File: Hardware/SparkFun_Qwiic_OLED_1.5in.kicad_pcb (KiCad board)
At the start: 2 copper layers, 34.3 x 49.5 mm, 69 parts, among them J1 Qwiic_RA, J2 Qwiic_RA, J4 Conn_01x24_FPC, J5 Conn_01x07, U2 WEO128128ASAP3N00000, U5 AP3012

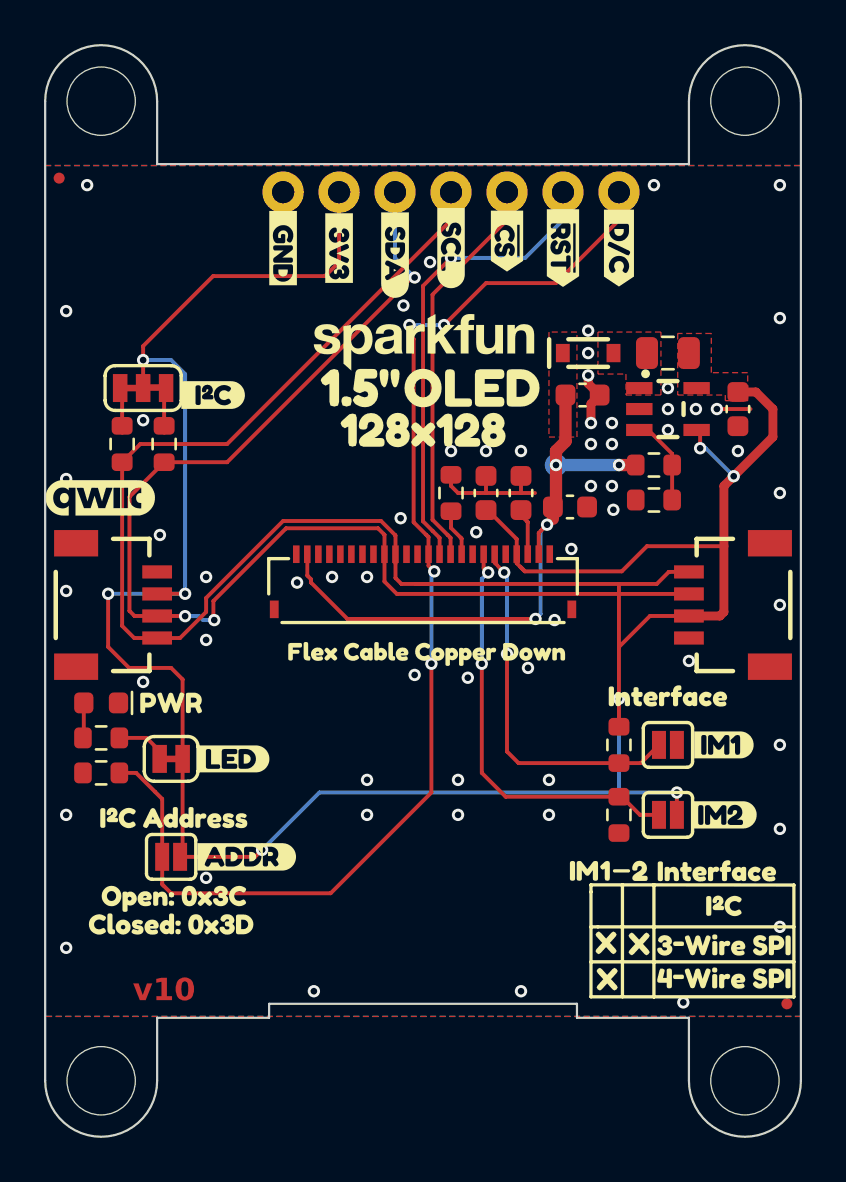
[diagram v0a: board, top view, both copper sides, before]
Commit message: Centers PTH headers and screen, fixes some DRC errors created by moving the FPC connector over that small amount
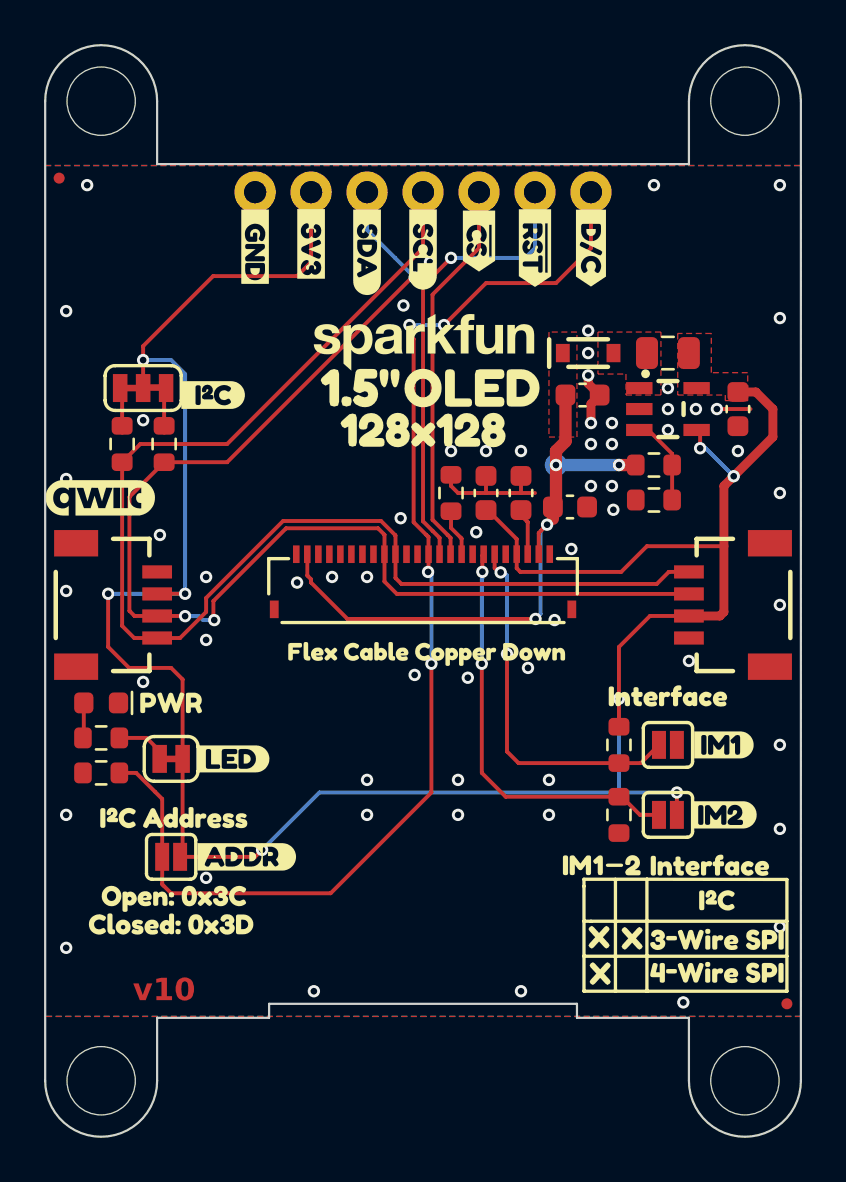
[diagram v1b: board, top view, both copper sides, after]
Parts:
- moved kibuzzard-67BF7ED9 1.28 mm to (135.3, 70.3)
- moved kibuzzard-67BF7F13 1.28 mm to (137.9, 70.7)
- moved kibuzzard-67BF7EBF 1.27 mm to (132.8, 70.4)
- moved kibuzzard-67BF7F2F 1.27 mm to (140.4, 70.5)
- moved J5 1.27 mm to (132.8, 67.9)
- moved kibuzzard-680E7A69 1.27 mm to (143.0, 70.2)
- moved kibuzzard-680E7A4B 1.27 mm to (145.5, 70.5)
- moved kibuzzard-685B1775 1.27 mm to (148.0, 70.5)
- moved kibuzzard-6893822D 0.41 mm to (147.4, 98.5)
- moved kibuzzard-689381EF 0.41 mm to (148.4, 103.4)
- moved kibuzzard-689381EF 0.41 mm to (148.4, 101.8)
- moved kibuzzard-68938236 0.41 mm to (148.3, 98.5)
- moved kibuzzard-68938244 0.41 mm to (153.4, 98.5)
- moved kibuzzard-6893824B 0.41 mm to (149.9, 98.5)
- moved kibuzzard-68938257 0.41 mm to (153.7, 100.1)
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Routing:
- net 3.3V: track 116.7 -> 112.5 mm
- net SCL/SCK: track 59.7 -> 58.7 mm
- net ~{CS}: track 18.2 -> 17.6 mm
- net ~{RST}: track 21.3 -> 20.8 mm
- net SDA/SDI: track 56.9 -> 57.4 mm

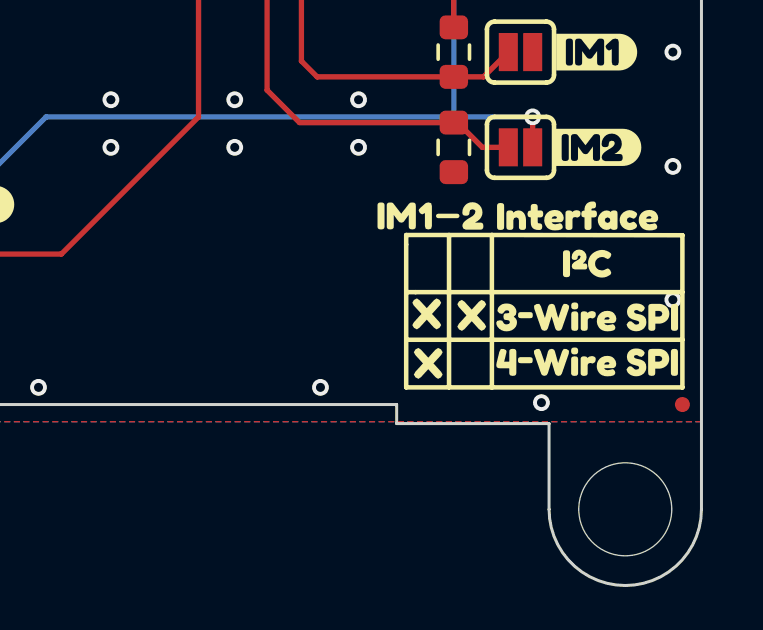
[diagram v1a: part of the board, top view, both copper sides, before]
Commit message: Adds some "O"'s to indicate open on the interface table
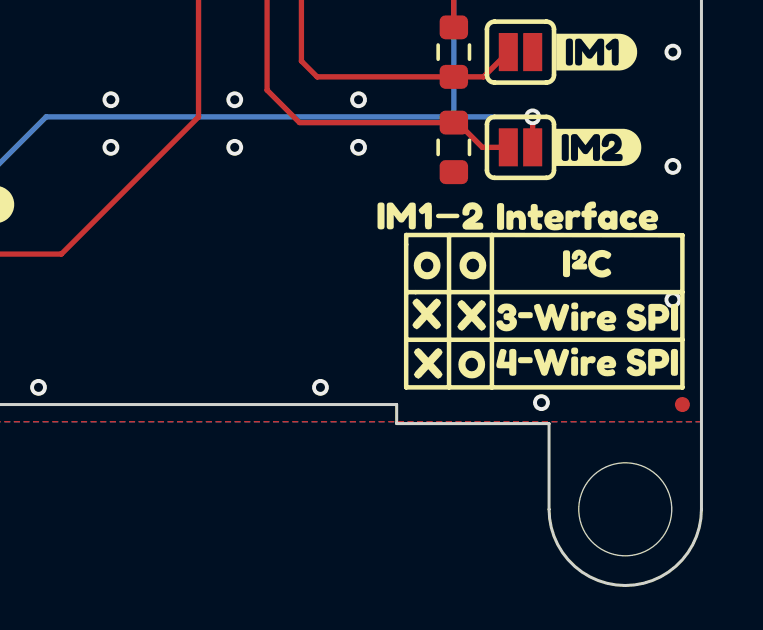
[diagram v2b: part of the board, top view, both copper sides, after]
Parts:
- added kibuzzard-6893A61C: G***, kibuzzard-6893A61C, F.Cu at (148.4, 100.1)
- added kibuzzard-6893A61C: G***, kibuzzard-6893A61C, F.Cu at (149.9, 103.4)
- added kibuzzard-6893A61C: G***, kibuzzard-6893A61C, F.Cu at (149.9, 100.1)
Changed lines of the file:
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@@
 		(embedded_fonts no)
 	)
+	(footprint "kibuzzard-6893A61C"
+		(layer "F.Cu")
+		(at 148.412 100.138)
+		(descr "Generated with KiBuzzard")
+		(tags "kb_params=eyJBbGlnbm1lbnRDaG9pY2UiOiAiQ2VudGVyIiwgIkNhcExlZnRDaG9pY2UiOiAiKCIsICJDYXBSaWdodENob2ljZSI6ICJdIiwgIkZvbnRDb21ib0JveCI6ICJGcmVkZHlTcGFyay1SZWd1bGFyIiwgIkhlaWdodEN0cmwiOiAwLjksICJMYXllckNvbWJvQm94IjogIkYuU2lsa1MiLCAiTGluZVNwYWNpbmdDdHJsIjogMS41LCAiTXVsdGlMaW5lVGV4dCI6ICJPIiwgIlBhZGRpbmdCb3R0b21DdHJsIjogMS41LCAiUGFkZGluZ0xlZnRDdHJsIjogMy4wLCAiUGFkZGluZ1JpZ2h0Q3RybCI6IDAuMCwgIlBhZGRpbmdUb3BDdHJsIjogMS41LCAiV2lkdGhDdHJsIjogMS4wLCAiYWR2YW5jZWRDaGVja2JveCI6IHRydWUsICJpbmxpbmVGb3JtYXRUZXh0Ym94IjogdHJ1ZSwgImxpbmVvdmVyU3R5bGVDaG9pY2UiOiAiU3F1YXJlIiwgImxpbmVvdmVyVGhpY2tuZXNzQ3RybCI6IDF9")
+		(property "Reference" "kibuzzard-6893A61C"
+			(at 0 -3.510876 0)
+			(layer "F.SilkS")
+			(hide yes)
+			(effects
+				(font
+					(size 0.001 0.001)
+				)
+			)
+		)
+		(property "Value" "G***"
+			(at 0 3.510876 0)
+			(layer "F.SilkS")
+			(hide yes)
+			(effects
+				(font
+					(size 0.001 0.001)
+				)
+			)
+		)
+		(property "Datasheet" ""
+			(at 0 0 0)
+			(layer "F.Fab")
+			(hide yes)
+			(effects
+				(font
+					(size 1.27 1.27)
+					(thickness 0.15)
+				)
+			)
+		)
+		(property "Description" ""
+			(at 0 0 0)
+			(layer "F.Fab")
+			(hide yes)
+			(effects
+				(font
+					(size 1.27 1.27)
+					(thickness 0.15)
+				)
+			)
+		)
+		(attr board_only exclude_from_pos_files exclude_from_bom)
+		(fp_poly
+			(pts
+				(xy 0.005794 0.462876) (xy -0.000644 0.462277) (xy -0.000644 0.227253) (xy 0.081277 0.210998) (xy 0.149356 0.162232)
+				(xy 0.195225 0.089324) (xy 0.210515 0.000644) (xy 0.195064 -0.087393) (xy 0.148712 -0.160944) (xy 0.080794 -0.210676)
+				(xy 0.000644 -0.227253) (xy -0.080472 -0.210676) (xy -0.148712 -0.160944) (xy -0.195064 -0.087393)
+				(xy -0.210515 0.000644) (xy -0.194903 0.08691) (xy -0.148069 0.1603) (xy -0.079989 0.210515) (xy -0.000644 0.227253)
+				(xy -0.000644 0.462277) (xy -0.084174 0.454506) (xy -0.167382 0.429399) (xy -0.24383 0.387554) (xy -0.313519 0.32897)
+				(xy -0.37154 0.258557) (xy -0.412983 0.181223) (xy -0.437849 0.096969) (xy -0.446137 0.005794) (xy -0.43809 -0.088358)
+				(xy -0.413948 -0.175107) (xy -0.373712 -0.254453) (xy -0.317382 -0.326395) (xy -0.249544 -0.386105)
+				(xy -0.174785 -0.428755) (xy -0.093106 -0.454345) (xy -0.004506 -0.462876) (xy 0.085944 -0.454466)
+				(xy 0.169313 -0.429238) (xy 0.245601 -0.387192) (xy 0.314807 -0.328326) (xy 0.372264 -0.25731) (xy 0.413305 -0.178809)
+				(xy 0.437929 -0.092825) (xy 0.446137 0.000644) (xy 0.43805 0.092503) (xy 0.413788 0.177521) (xy 0.37335 0.2557)
+				(xy 0.316738 0.327039) (xy 0.24878 0.386467) (xy 0.174303 0.428916) (xy 0.093307 0.454386) (xy 0.005794 0.462876)
+			)
+			(stroke
+				(width 0)
+				(type solid)
+			)
+			(fill yes)
+			(layer "F.SilkS")
+		)
+		(embedded_fonts no)
+	)
 	(footprint "SparkFun-Resistor:R_0603_1608Metric"
 		(layer "F.Cu")
@@
 		)
 	)
+	(footprint "kibuzzard-6893A61C"
+		(layer "F.Cu")
+		(at 149.8985 103.44)
+		(descr "Generated with KiBuzzard")
+		(tags "kb_params=eyJBbGlnbm1lbnRDaG9pY2UiOiAiQ2VudGVyIiwgIkNhcExlZnRDaG9pY2UiOiAiKCIsICJDYXBSaWdodENob2ljZSI6ICJdIiwgIkZvbnRDb21ib0JveCI6ICJGcmVkZHlTcGFyay1SZWd1bGFyIiwgIkhlaWdodEN0cmwiOiAwLjksICJMYXllckNvbWJvQm94IjogIkYuU2lsa1MiLCAiTGluZVNwYWNpbmdDdHJsIjogMS41LCAiTXVsdGlMaW5lVGV4dCI6ICJPIiwgIlBhZGRpbmdCb3R0b21DdHJsIjogMS41LCAiUGFkZGluZ0xlZnRDdHJsIjogMy4wLCAiUGFkZGluZ1JpZ2h0Q3RybCI6IDAuMCwgIlBhZGRpbmdUb3BDdHJsIjogMS41LCAiV2lkdGhDdHJsIjogMS4wLCAiYWR2YW5jZWRDaGVja2JveCI6IHRydWUsICJpbmxpbmVGb3JtYXRUZXh0Ym94IjogdHJ1ZSwgImxpbmVvdmVyU3R5bGVDaG9pY2UiOiAiU3F1YXJlIiwgImxpbmVvdmVyVGhpY2tuZXNzQ3RybCI6IDF9")
+		(property "Reference" "kibuzzard-6893A61C"
+			(at 0 -3.510876 0)
+			(layer "F.SilkS")
+			(hide yes)
+			(effects
+				(font
+					(size 0.001 0.001)
+					(thickness 0.15)
+				)
+			)
+		)
+		(property "Value" "G***"
+			(at 0 3.510876 0)
+			(layer "F.SilkS")
+			(hide yes)
+			(effects
+				(font
+					(size 0.001 0.001)
+					(thickness 0.15)
+				)
+			)
+		)
+		(property "Datasheet" ""
+			(at 0 0 0)
+			(layer "F.Fab")
+			(hide yes)
+			(effects
+				(font
+					(size 1.27 1.27)
+					(thickness 0.15)
+				)
+			)
+		)
+		(property "Description" ""
+			(at 0 0 0)
+			(layer "F.Fab")
+			(hide yes)
+			(effects
+				(font
+					(size 1.27 1.27)
+					(thickness 0.15)
+				)
+			)
+		)
+		(attr board_only exclude_from_pos_files exclude_from_bom)
+		(fp_poly
+			(pts
+				(xy 0.005794 0.462876) (xy -0.000644 0.462277) (xy -0.000644 0.227253) (xy 0.081277 0.210998) (xy 0.149356 0.162232)
+				(xy 0.195225 0.089324) (xy 0.210515 0.000644) (xy 0.195064 -0.087393) (xy 0.148712 -0.160944) (xy 0.080794 -0.210676)
+				(xy 0.000644 -0.227253) (xy -0.080472 -0.210676) (xy -0.148712 -0.160944) (xy -0.195064 -0.087393)
+				(xy -0.210515 0.000644) (xy -0.194903 0.08691) (xy -0.148069 0.1603) (xy -0.079989 0.210515) (xy -0.000644 0.227253)
+				(xy -0.000644 0.462277) (xy -0.084174 0.454506) (xy -0.167382 0.429399) (xy -0.24383 0.387554) (xy -0.313519 0.32897)
+				(xy -0.37154 0.258557) (xy -0.412983 0.181223) (xy -0.437849 0.096969) (xy -0.446137 0.005794) (xy -0.43809 -0.088358)
+				(xy -0.413948 -0.175107) (xy -0.373712 -0.254453) (xy -0.317382 -0.326395) (xy -0.249544 -0.386105)
+				(xy -0.174785 -0.428755) (xy -0.093106 -0.454345) (xy -0.004506 -0.462876) (xy 0.085944 -0.454466)
+				(xy 0.169313 -0.429238) (xy 0.245601 -0.387192) (xy 0.314807 -0.328326) (xy 0.372264 -0.25731) (xy 0.413305 -0.178809)
+				(xy 0.437929 -0.092825) (xy 0.446137 0.000644) (xy 0.43805 0.092503) (xy 0.413788 0.177521) (xy 0.37335 0.2557)
+				(xy 0.316738 0.327039) (xy 0.24878 0.386467) (xy 0.174303 0.428916) (xy 0.093307 0.454386) (xy 0.005794 0.462876)
+			)
+			(stroke
+				(width 0)
+				(type solid)
+			)
+			(fill yes)
+			(layer "F.SilkS")
+		)
+		(embedded_fonts no)
+	)
 	(footprint "SparkFun-Jumper:Jumper_3_NC-2_Trace"
 		(layer "F.Cu")
@@
 			)
 			(stroke
+				(width 0)
+				(type solid)
+			)
+			(fill yes)
+			(layer "F.SilkS")
+		)
+		(embedded_fonts no)
+	)
+	(footprint "kibuzzard-6893A61C"
+		(layer "F.Cu")
+		(at 149.936 100.138)
+		(descr "Generated with KiBuzzard")
+		(tags "kb_params=eyJBbGlnbm1lbnRDaG9pY2UiOiAiQ2VudGVyIiwgIkNhcExlZnRDaG9pY2UiOiAiKCIsICJDYXBSaWdodENob2ljZSI6ICJdIiwgIkZvbnRDb21ib0JveCI6ICJGcmVkZHlTcGFyay1SZWd1bGFyIiwgIkhlaWdodEN0cmwiOiAwLjksICJMYXllckNvbWJvQm94IjogIkYuU2lsa1MiLCAiTGluZVNwYWNpbmdDdHJsIjogMS41LCAiTXVsdGlMaW5lVGV4dCI6ICJPIiwgIlBhZGRpbmdCb3R0b21DdHJsIjogMS41LCAiUGFkZGluZ0xlZnRDdHJsIjogMy4wLCAiUGFkZGluZ1JpZ2h0Q3RybCI6IDAuMCwgIlBhZGRpbmdUb3BDdHJsIjogMS41LCAiV2lkdGhDdHJsIjogMS4wLCAiYWR2YW5jZWRDaGVja2JveCI6IHRydWUsICJpbmxpbmVGb3JtYXRUZXh0Ym94IjogdHJ1ZSwgImxpbmVvdmVyU3R5bGVDaG9pY2UiOiAiU3F1YXJlIiwgImxpbmVvdmVyVGhpY2tuZXNzQ3RybCI6IDF9")
+		(property "Reference" "kibuzzard-6893A61C"
+			(at 0 -3.510876 0)
+			(layer "F.SilkS")
+			(hide yes)
+			(effects
+				(font
+					(size 0.001 0.001)
+					(thickness 0.15)
+				)
+			)
+		)
+		(property "Value" "G***"
+			(at 0 3.510876 0)
+			(layer "F.SilkS")
+			(hide yes)
+			(effects
+				(font
+					(size 0.001 0.001)
+					(thickness 0.15)
+				)
+			)
+		)
+		(property "Datasheet" ""
+			(at 0 0 0)
+			(layer "F.Fab")
+			(hide yes)
+			(effects
+				(font
+					(size 1.27 1.27)
+					(thickness 0.15)
+				)
+			)
+		)
+		(property "Description" ""
+			(at 0 0 0)
+			(layer "F.Fab")
+			(hide yes)
+			(effects
+				(font
+					(size 1.27 1.27)
+					(thickness 0.15)
+				)
+			)
+		)
+		(attr board_only exclude_from_pos_files exclude_from_bom)
+		(fp_poly
+			(pts
+				(xy 0.005794 0.462876) (xy -0.000644 0.462277) (xy -0.000644 0.227253) (xy 0.081277 0.210998) (xy 0.149356 0.162232)
+				(xy 0.195225 0.089324) (xy 0.210515 0.000644) (xy 0.195064 -0.087393) (xy 0.148712 -0.160944) (xy 0.080794 -0.210676)
+				(xy 0.000644 -0.227253) (xy -0.080472 -0.210676) (xy -0.148712 -0.160944) (xy -0.195064 -0.087393)
+				(xy -0.210515 0.000644) (xy -0.194903 0.08691) (xy -0.148069 0.1603) (xy -0.079989 0.210515) (xy -0.000644 0.227253)
+				(xy -0.000644 0.462277) (xy -0.084174 0.454506) (xy -0.167382 0.429399) (xy -0.24383 0.387554) (xy -0.313519 0.32897)
+				(xy -0.37154 0.258557) (xy -0.412983 0.181223) (xy -0.437849 0.096969) (xy -0.446137 0.005794) (xy -0.43809 -0.088358)
+				(xy -0.413948 -0.175107) (xy -0.373712 -0.254453) (xy -0.317382 -0.326395) (xy -0.249544 -0.386105)
+				(xy -0.174785 -0.428755) (xy -0.093106 -0.454345) (xy -0.004506 -0.462876) (xy 0.085944 -0.454466)
+				(xy 0.169313 -0.429238) (xy 0.245601 -0.387192) (xy 0.314807 -0.328326) (xy 0.372264 -0.25731) (xy 0.413305 -0.178809)
+				(xy 0.437929 -0.092825) (xy 0.446137 0.000644) (xy 0.43805 0.092503) (xy 0.413788 0.177521) (xy 0.37335 0.2557)
+				(xy 0.316738 0.327039) (xy 0.24878 0.386467) (xy 0.174303 0.428916) (xy 0.093307 0.454386) (xy 0.005794 0.462876)
+			)
+			(stroke

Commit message: Adds "I2C" to address in schematic, removes stub
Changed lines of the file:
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@@
 				(font
 					(size 0.001 0.001)
+					(thickness 0.15)
 				)
 			)
@@
 				(font
 					(size 0.001 0.001)
+					(thickness 0.15)
 				)
 			)
@@
 				(font
 					(size 0.001 0.001)
+					(thickness 0.15)
 				)
 			)
@@
 				(font
 					(size 0.001 0.001)
+					(thickness 0.15)
 				)
 			)
@@
 				(font
 					(size 0.001 0.001)
+					(thickness 0.15)
 				)
 			)
@@
 				(font
 					(size 0.001 0.001)
+					(thickness 0.15)
 				)
 			)
@@
 				(font
 					(size 0.001 0.001)
+					(thickness 0.15)
 				)
 			)
@@
 				(font
 					(size 0.001 0.001)
+					(thickness 0.15)
 				)
 			)
@@
 				(font
 					(size 0.001 0.001)
+					(thickness 0.15)
 				)
 			)
@@
 				(font
 					(size 0.001 0.001)
+					(thickness 0.15)
 				)
 			)
@@
 				(font
 					(size 0.001 0.001)
+					(thickness 0.15)
 				)
 			)
@@
 				(font
 					(size 0.001 0.001)
+					(thickness 0.15)
 				)
 			)
@@
 				(font
 					(size 0.001 0.001)
+					(thickness 0.15)
 				)
 			)
@@
 				(font
 					(size 0.001 0.001)
+					(thickness 0.15)
 				)
 			)
@@
 				(font
 					(size 0.001 0.001)
+					(thickness 0.15)
 				)
 			)
@@
 				(font
 					(size 0.001 0.001)
+					(thickness 0.15)
 				)
 			)
@@
 				(font
 					(size 0.001 0.001)
+					(thickness 0.15)
 				)
 			)
@@
 				(font
 					(size 0.001 0.001)
+					(thickness 0.15)
 				)
 			)
@@
 		(width 0.1778)
 		(layer "F.Cu")
-		(net 22)
-	)
-	(segment
-		(start 143.104 85.171985)
-		(end 143.104 85.052679)
-		(width 0.1778)
-		(layer "F.Cu")

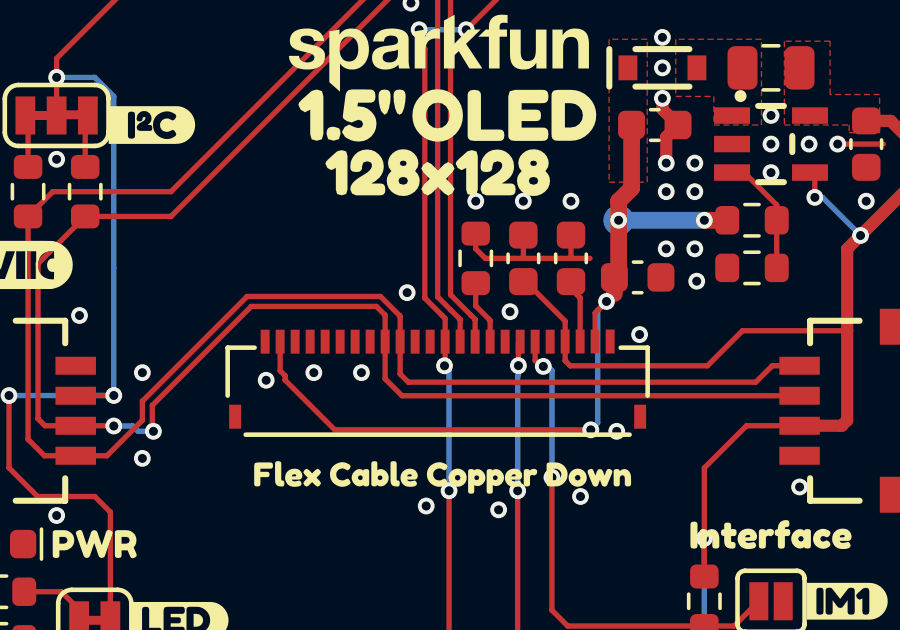
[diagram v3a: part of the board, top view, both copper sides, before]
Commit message: Moves the connector up .05" so that the FPC cable is a bit tighter to the PCB when the screen is secured ot it
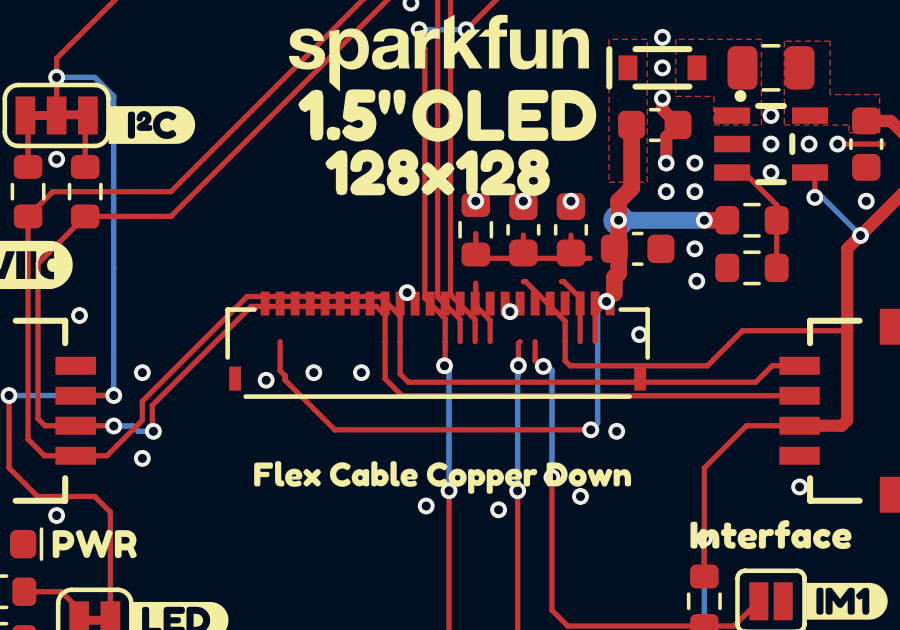
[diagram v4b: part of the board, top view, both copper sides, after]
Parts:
- moved U2 1.71 mm to (140.4, 85.7)
- moved J4 1.27 mm to (140.4, 84.5)
- moved C3 0.95 mm to (144.9, 80.6)
- moved C4 0.95 mm to (143.3, 80.6)
- moved C5 0.95 mm to (147.1, 81.3)
- moved R6 0.95 mm to (141.7, 80.6)
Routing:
- net GND: vias 61 -> 60
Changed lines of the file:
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@@
 	(footprint "SparkFun-Resistor:R_0603_1608Metric"
 		(layer "F.Cu")
-		(at 141.681 81.596 -90)
+		(at 141.681 80.6435 -90)
 		(descr "Resistor SMD 0603 (1608 Metric), square (rectangular) end terminal, IPC_7351 nominal, (Body size source: IPC-SM-782 page 72, https://www.pcb-3d.com/wordpress/wp-content/uploads/ipc-sm-782a_amendment_1_and_2.pdf), generated with kicad-footprint-generator")
 		(tags "SparkFun resistor")
@@
 	(footprint "SparkFun-Capacitor:C_0603_1608Metric"
 		(layer "F.Cu")
-		(at 147.0785 82.231)
+		(at 147.0785 81.2785)
 		(tags "SparkFun capacitor")
 		(property "Reference" "C5"
@@
 	(footprint "SparkFun-Capacitor:C_0603_1608Metric"
 		(layer "F.Cu")
-		(at 143.2685 81.596 90)
+		(at 143.2685 80.6435 90)
 		(tags "SparkFun capacitor")
 		(property "Reference" "C4"
@@
 	(footprint "SparkFun-Connector:FPC_0.5mm-24"
 		(layer "F.Cu")
-		(at 140.4109 85.7235)
+		(at 140.4109 84.4535)
 		(tags "SparkFun 24 pin 0.5mm dual contact back flip connector")
 		(property "Reference" "J4"
@@
 	(footprint "SparkFun-Capacitor:C_0603_1608Metric"
 		(layer "F.Cu")
-		(at 144.856 81.596 90)
+		(at 144.856 80.6435 90)
 		(tags "SparkFun capacitor")
 		(property "Reference" "C3"
@@
 	)
 	(footprint "SparkFun-Display:OLED_1.5in_128x128-Folded"
-		(locked yes)
 		(layer "F.Cu")
-		(at 140.411 87.3955)
+		(at 140.411 85.681)
 		(tags "SparkFun OLED 1.5\" 128 x 128")
 		(property "Reference" "U2"
@@
 		(size 0.56)
 		(drill 0.3)
-		(layers "F.Cu" "B.Cu")
-		(free yes)
-		(net 2)
-	)
-	(via
-		(at 148.031 81.2785)
-		(size 0.56)
-		(drill 0.3)
